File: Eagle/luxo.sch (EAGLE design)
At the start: 16 parts, among them IC1 3.3

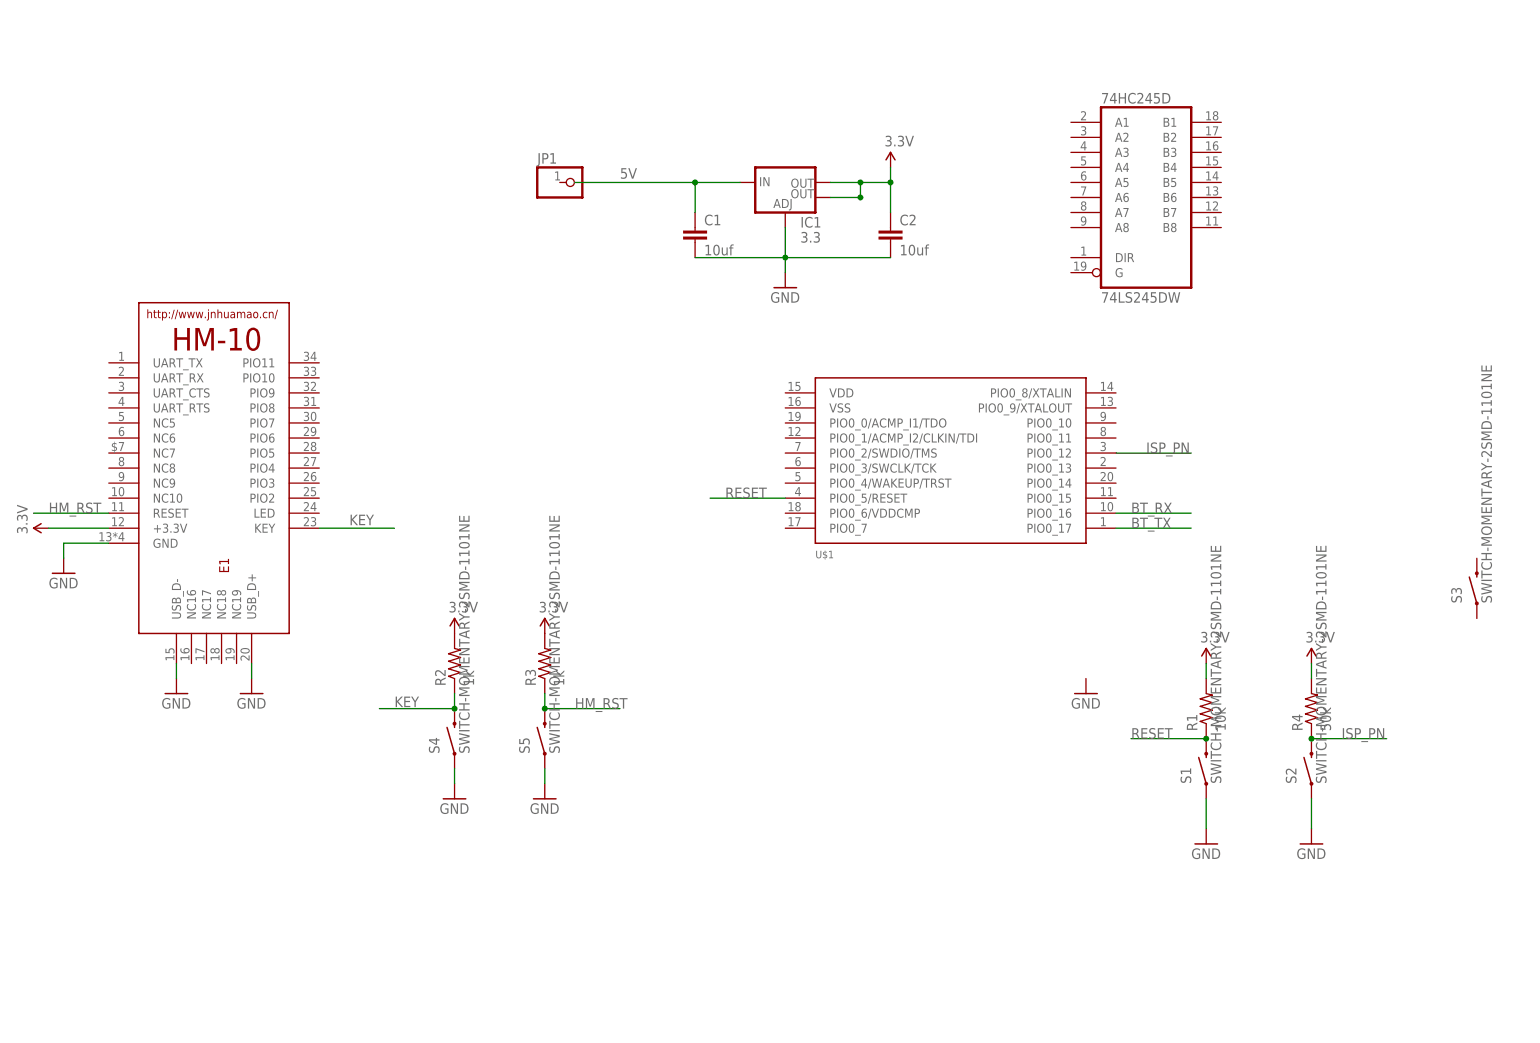
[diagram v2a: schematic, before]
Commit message: Add 74HCT245 level shifter
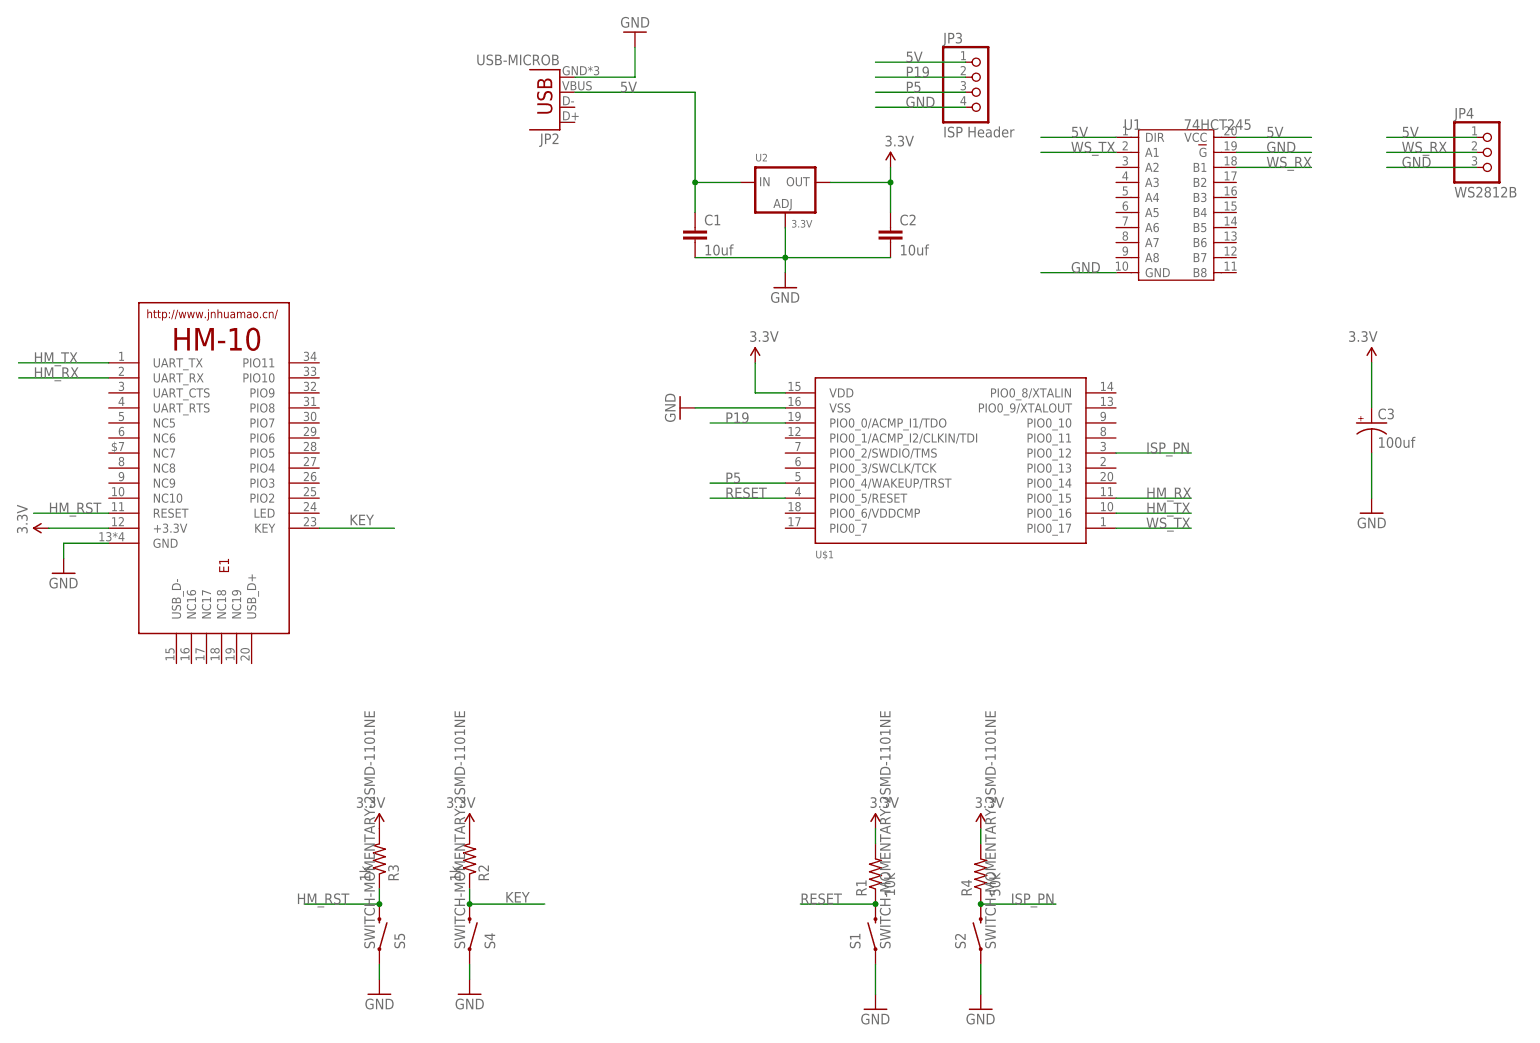
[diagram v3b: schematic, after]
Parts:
- removed 74HC245D: 74LS245DW, 74xx-us:74LS245DW
- removed IC1: 3.3, SparkFun-PowerIC:V_REG_LM1117SOT223
- removed JP1: (no value), adafruit:PINHD-1X1
- removed S3: SWITCH-MOMENTARY-2SMD-1101NE, SparkFun-Electromechanical:SWITCH-MOMENTARY-2SMD-1101NE
- added C3: 100uf, SparkFun-Capacitors:100UF-25V-20%(PTH)
- added JP2: USB-MICROB, SparkFun-Connectors:USB-MICROB
- added JP3: ISP Header, microbuilder:HEADER-1X4ROUND
- added JP4: WS2812B, microbuilder:HEADER-1X3
- added U1: 74HCT245, TFT Touch:74ACT245-SOP20
- added U2: 3.3V, microbuilder:LM1117SOT223-WAVE
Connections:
- removed net BT_RX: U$1.PIO0_16
- removed net BT_TX: U$1.PIO0_17
- new net HM_RX: E1.UART_RX, U$1.PIO0_15
- new net HM_TX: E1.UART_TX, U$1.PIO0_16
- new net P19: JP3.2, U$1.PIO0_0/ACMP_I1/TDO
- new net P5: JP3.3, U$1.PIO0_4/WAKEUP/TRST
- new net WS_RX: JP4.2, U1.B1
- new net WS_TX: U$1.PIO0_17, U1.A1
- net 3.3V: now also C3.+, U$1.VDD, U2.OUT; no longer IC1.OUT, IC1.OUT@1
- net 5V: now also JP2.VBUS, JP3.1, JP4.1, U1.DIR, U1.VCC, U2.IN; no longer IC1.IN
- net GND: now also C3.-, JP2.GND, JP3.4, JP4.3, U$1.VSS, U1.G, U1.GND, U2.ADJ; no longer IC1.ADJ
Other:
- moved on the sheet: R1, R2, R3, R4, S1, S2, S4, S5
